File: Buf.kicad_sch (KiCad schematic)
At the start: 28 parts, among them U13 74AHCT573PW, U15 74AHCT573PW, U16 74AHCT573PW, U17 74AHCT573PW, U18 74AHCT573PW, U19 74AHCT573PW, U2 74AHCT573PW, U20 74AHCT573PW, U21 74AHCT573PW, U22 74AHCT573PW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

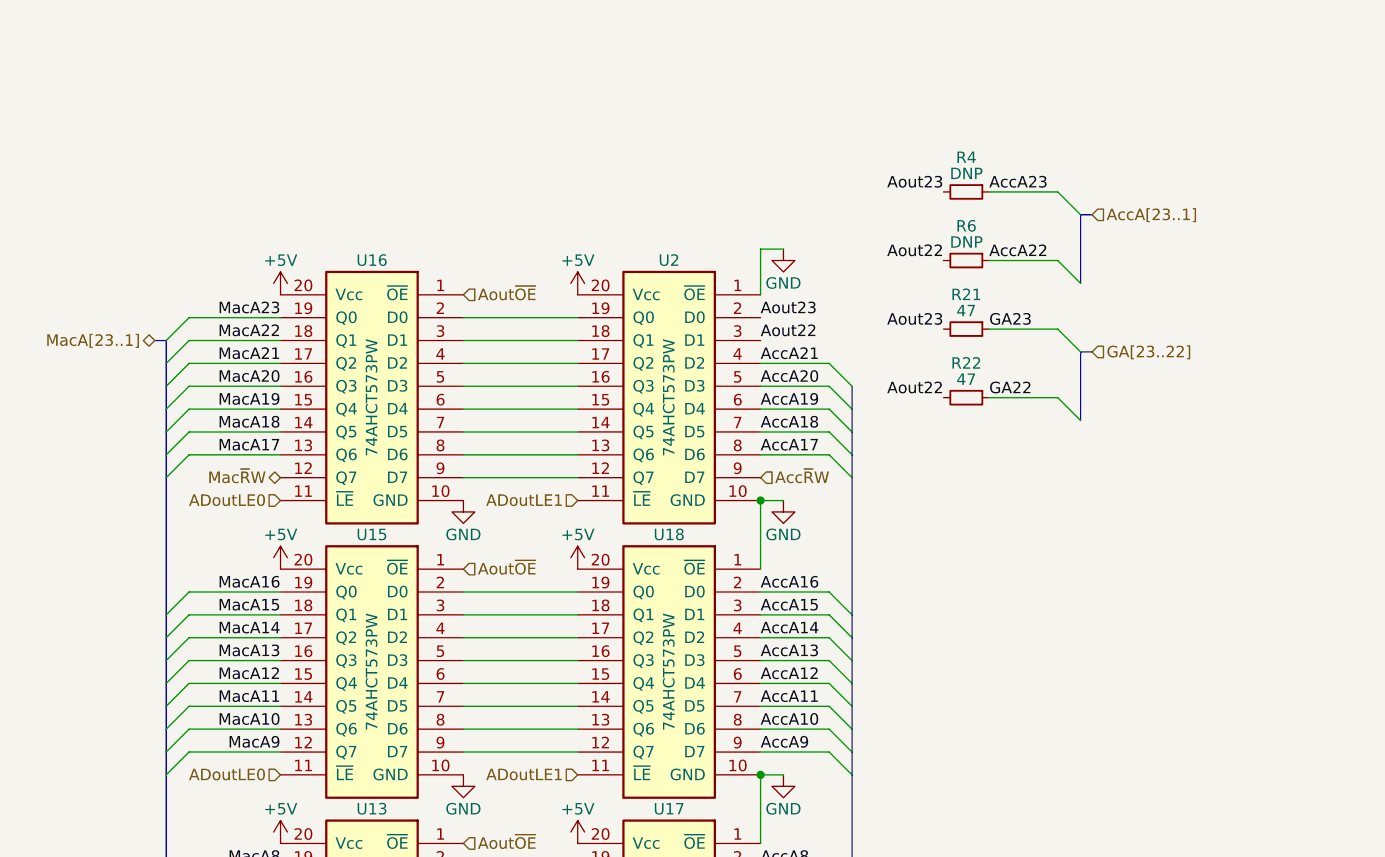
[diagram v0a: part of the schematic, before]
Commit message: Board prerelease revision 3 with USB power, A[23:20] remapping
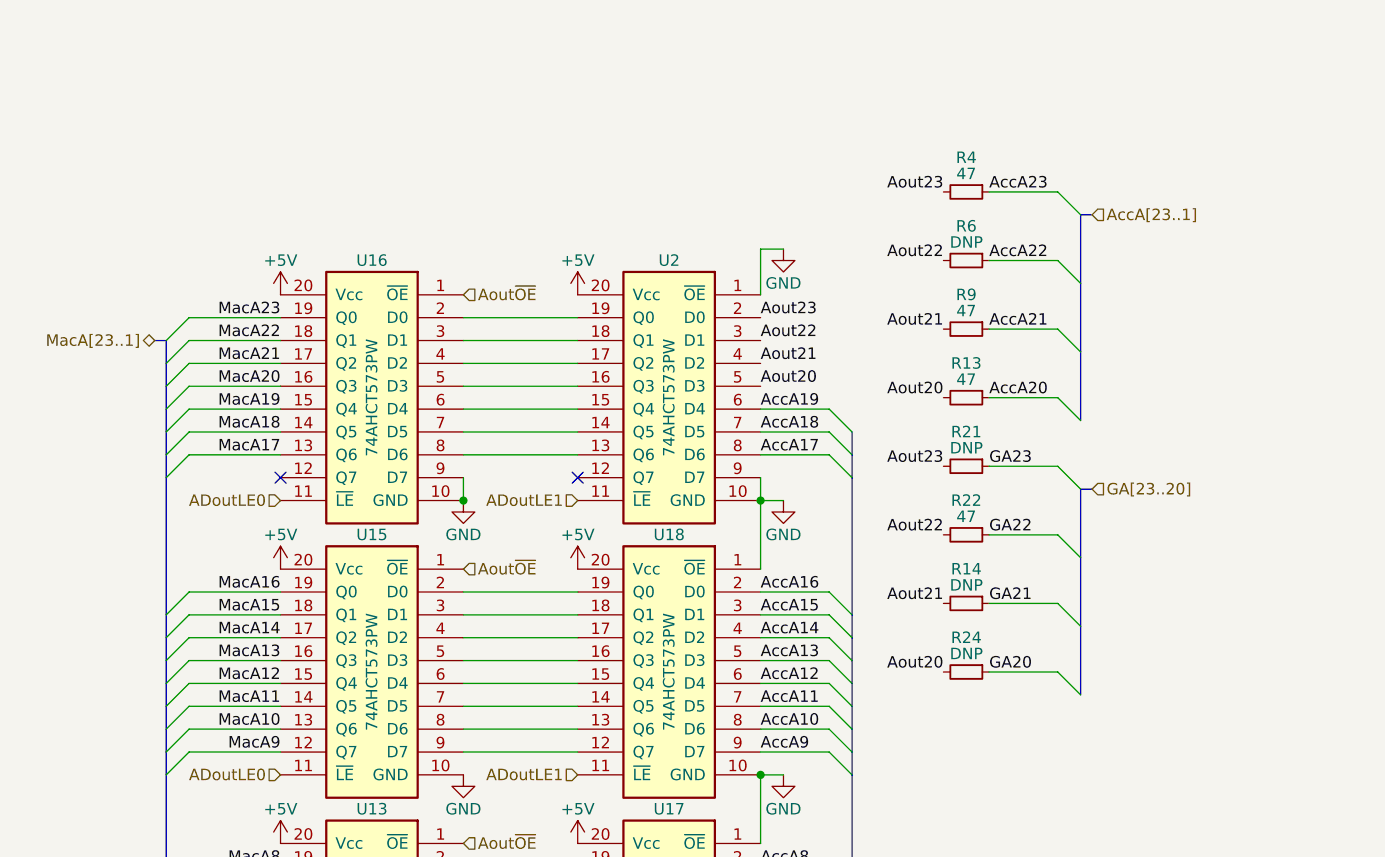
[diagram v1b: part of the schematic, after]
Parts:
- added R13, R9: 47, stdpads:R_0603, symbol Device:R_Small
- added R14, R24: DNP, stdpads:R_0603, symbol Device:R_Small
- R21: value 47 -> DNP; LCSC Part C23182 -> (none)
- R4: value DNP -> 47; LCSC Part (none) -> C23182
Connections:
- net Acc~{R}W is gone; now on net GND: U2.9 (D7)
- net AccA20: now also R13.1; no longer U2.5 (D3)
- net AccA21: now also R9.1; no longer U2.4 (D2)
- net GND: now also U16.9 (D7)
- net at U2.12 (Q7): no longer U16.9 (D7)
- net Mac~{R}W: no longer names the net of U16.12 (Q7)
- new net Aout20: R13.2, R24.2, U2.5 (D3)
- new net Aout21: R14.2, R9.2, U2.4 (D2)
- new net GA20: R24.1
- new net GA21: R14.1
- no-connect marks 0 -> 2
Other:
- moved on the sheet: R22
